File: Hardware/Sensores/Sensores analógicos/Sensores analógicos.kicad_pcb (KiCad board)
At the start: 2 copper layers, 3 parts, among them J1 Sensores de Corriente, J2 Screw_Terminal_01x07, U1 MCP3008

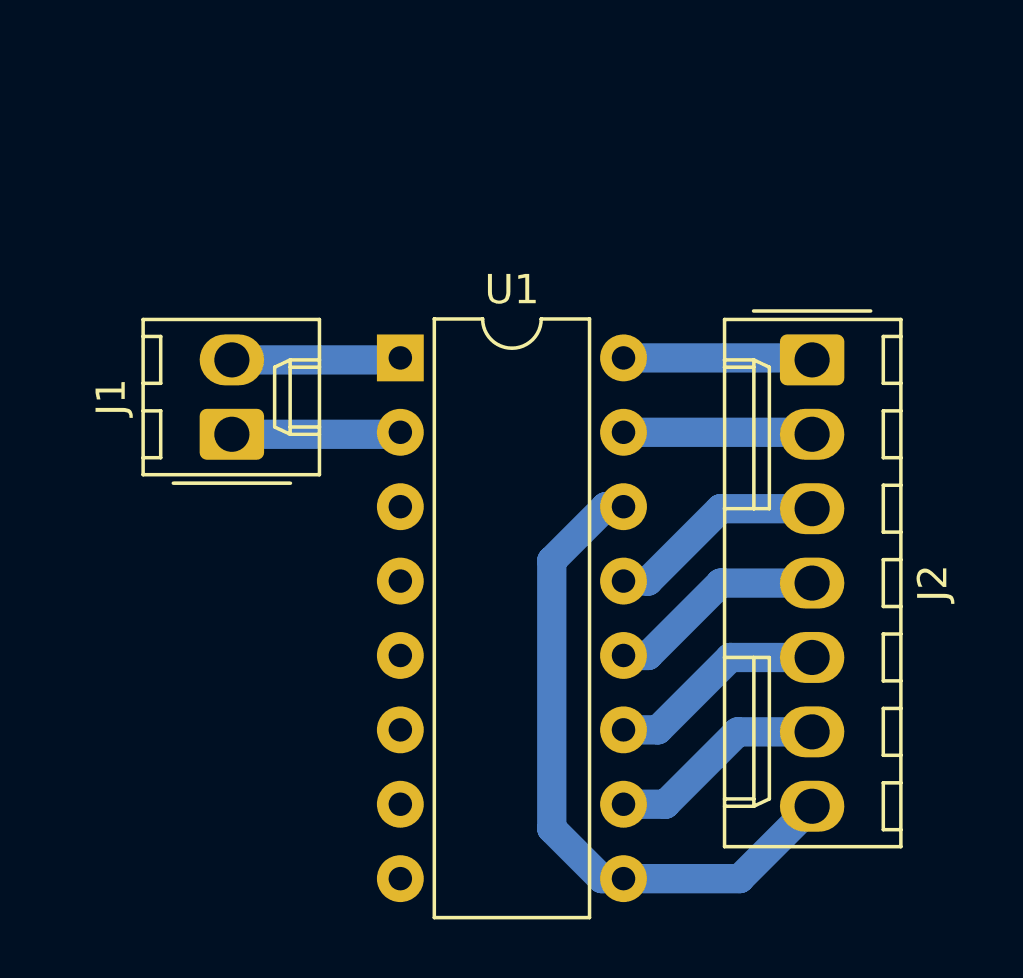
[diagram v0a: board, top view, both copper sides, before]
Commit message: PCB Sensor de porcentaje de bateria
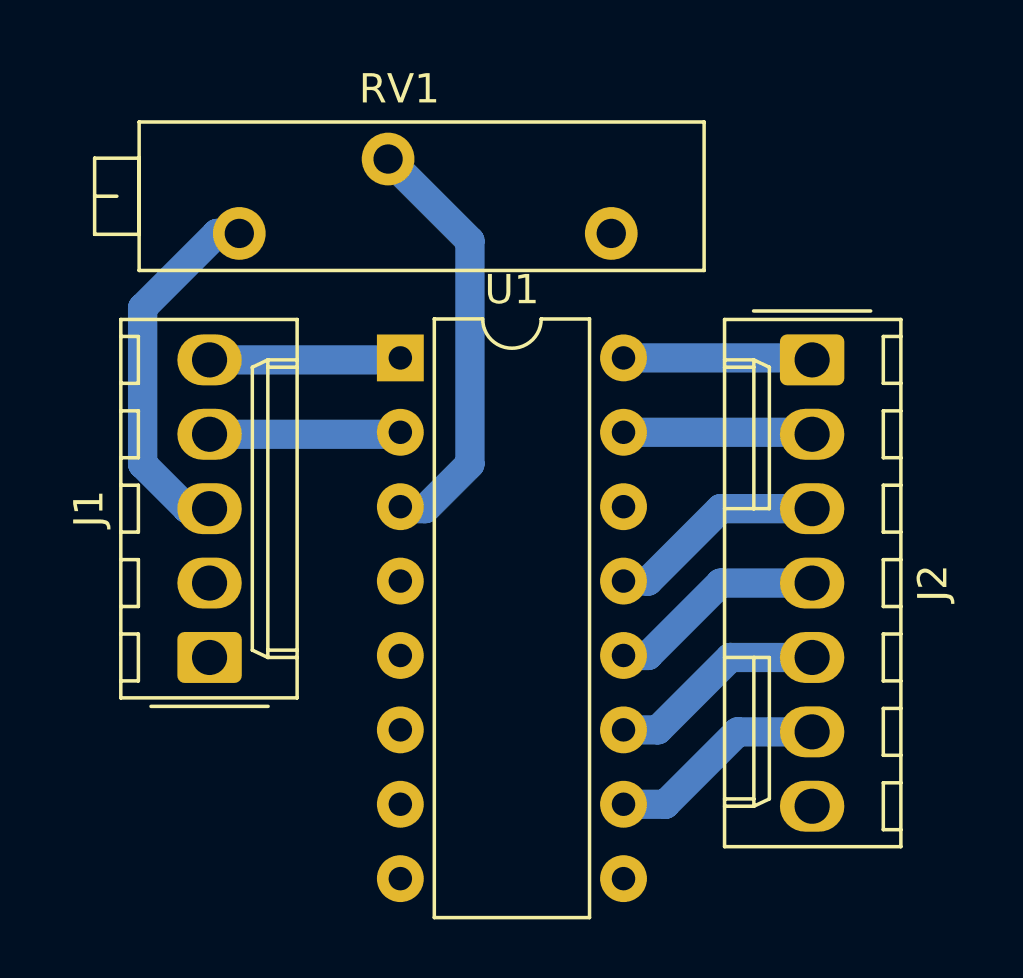
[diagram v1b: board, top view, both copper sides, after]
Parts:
- added RV1: 500k, Potentiometer_THT:Potentiometer_Bourns_3006P_Horizontal, F.Cu at (132.3, 68.6)
- J1: value Sensores de Corriente -> Entradas X5; footprint Connector_Molex:Molex_KK-254_AE-6410-02A_1x02_P2.54mm_Vertical -> Connector_Molex:Molex_KK-254_AE-6410-05A_1x05_P2.54mm_Vertical
- moved J1 7.66 mm to (118.6, 83.1)
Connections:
- net Net-(J2-Pad7) renamed Earth
- U1 pad 1: Net-(J1-Pad2) -> Net-(J1-Pad5)
- U1 pad 2: Net-(J1-Pad1) -> Net-(J1-Pad4)
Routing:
- net Earth: track 23.0 -> 0.00 mm
- net Net-(RV1-Pad2): track 0.00 -> 14.6 mm
- net Net-(J1-Pad3): track 0.00 -> 12.6 mm
- net Net-(J1-Pad5): track 0.00 -> 6.54 mm
- net Net-(J1-Pad4): track 0.00 -> 6.54 mm
- net Net-(J1-Pad2): track 5.78 -> 0.00 mm
- net Net-(J1-Pad1): track 5.78 -> 0.00 mm
